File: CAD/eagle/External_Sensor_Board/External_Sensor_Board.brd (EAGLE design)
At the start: 50.8 x 33 mm, 12 parts, among them J1 SFW15R_FFC, U1 MAX31725MTA+, U2 HSCMNNN1.6BAAA3

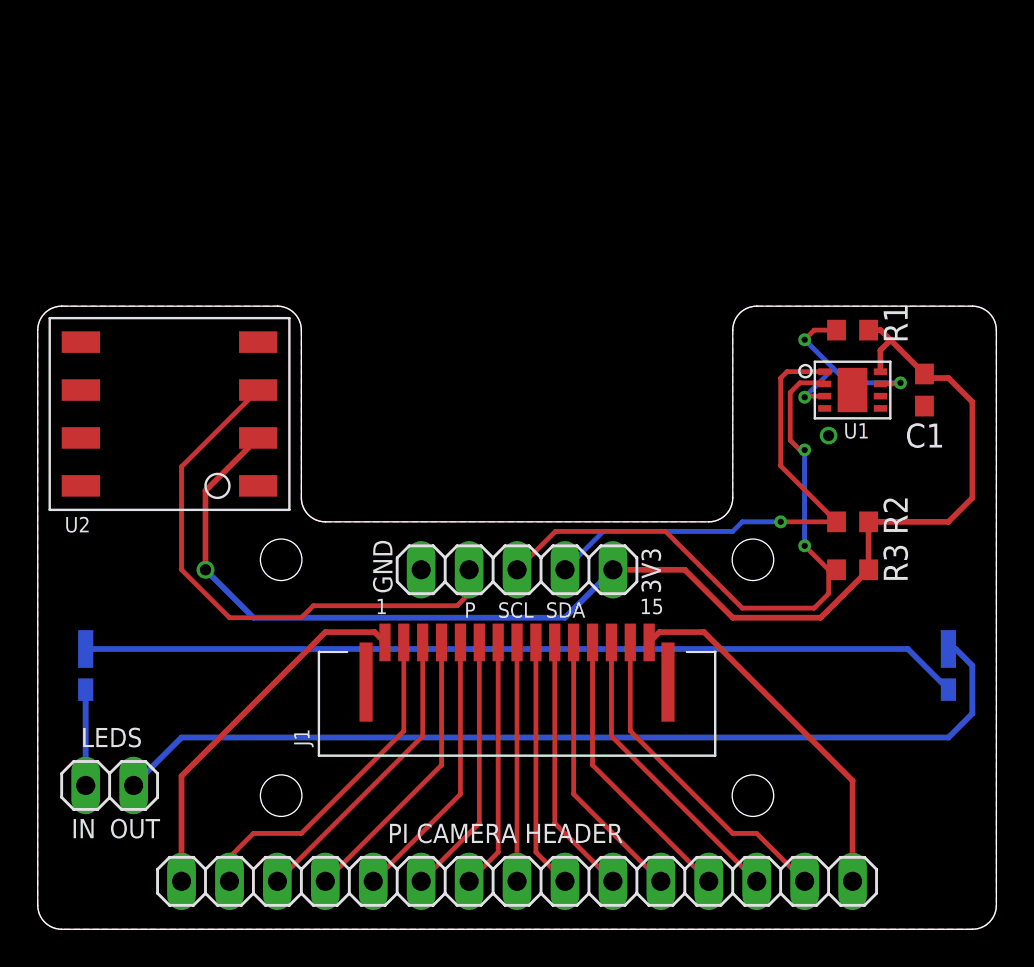
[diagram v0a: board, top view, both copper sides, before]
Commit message: Fixed dumb mistake on external sensor board, screw holes are now right distance apart. Rerouted around hole placement and verfied that DRC was still okay.
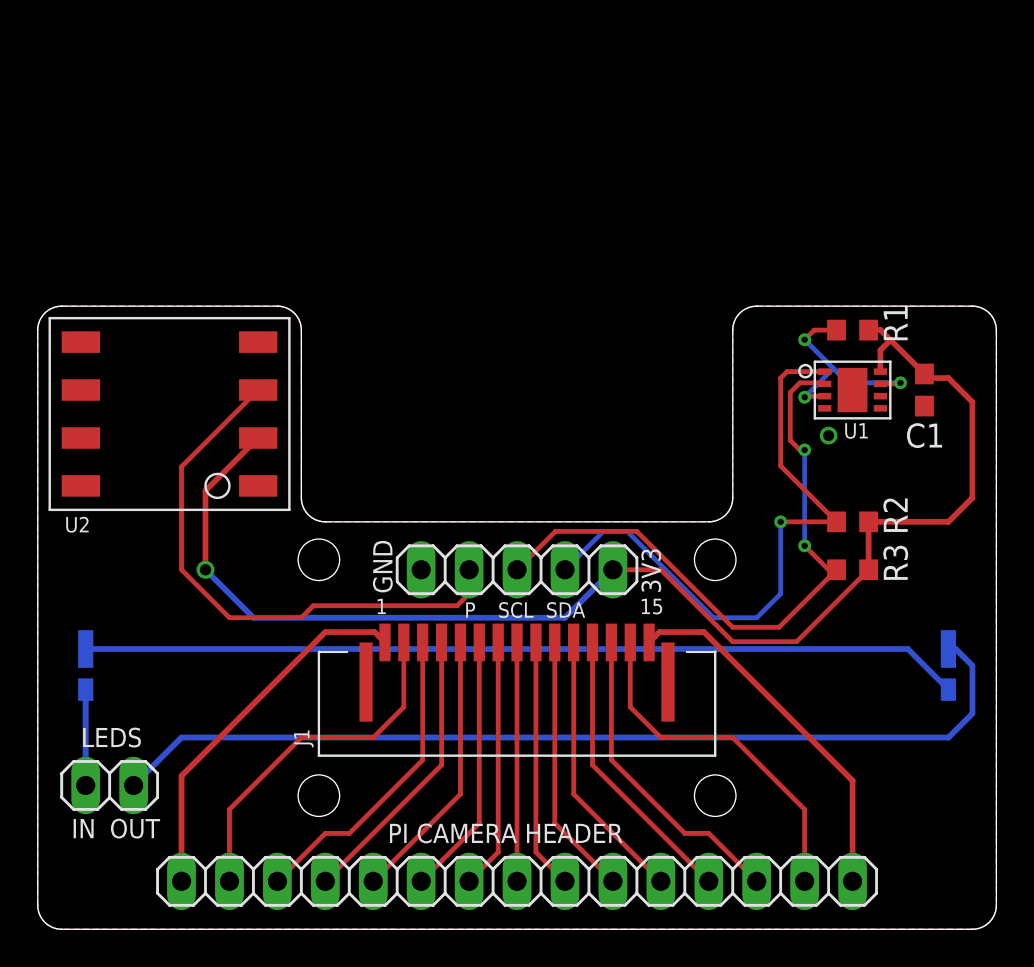
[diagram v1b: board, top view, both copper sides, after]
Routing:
- net SDA: track 26.8 -> 32.8 mm
- net CAM_SDA: track 17.2 -> 18.7 mm
- net +3V3: track 70.1 -> 71.2 mm
- net CAM_DP0: track 15.8 -> 16.6 mm
- net CAM_DN0: track 18.0 -> 18.7 mm
- net CAM_SCL: track 15.8 -> 16.6 mm
- net SCL: track 33.5 -> 34.0 mm
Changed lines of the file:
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@@
 <setting verticaltext="up"/>
 </settings>
-<grid distance="0.05" unitdist="inch" unit="mm" style="lines" multiple="1" display="yes" altdistance="0.01" altunitdist="inch" altunit="inch"/>
+<grid distance="0.05" unitdist="inch" unit="inch" style="lines" multiple="1" display="yes" altdistance="0.01" altunitdist="inch" altunit="inch"/>
 <layers>
 <layer number="1" name="Top" color="4" fill="1" visible="yes" active="yes"/>
@@
 <wire x1="12.7" y1="33.02" x2="1.27" y2="33.02" width="0" layer="20"/>
 <wire x1="1.27" y1="33.02" x2="0" y2="31.75" width="0" layer="20" curve="90"/>
-<hole x="12.9" y="19.58" drill="2.2"/>
-<hole x="37.9" y="19.58" drill="2.2"/>
-<hole x="37.9" y="7.08" drill="2.2"/>
-<hole x="12.9" y="7.08" drill="2.2"/>
+<hole x="14.89836875" y="19.58" drill="2.2"/>
+<hole x="35.90163125" y="19.58" drill="2.2"/>
+<hole x="35.90163125" y="7.08" drill="2.2"/>
+<hole x="14.89836875" y="7.08" drill="2.2"/>
 <wire x1="15.24" y1="21.59" x2="35.56" y2="21.59" width="0" layer="20"/>
 <wire x1="35.56" y1="21.59" x2="36.83" y2="22.86" width="0" layer="20" curve="90"/>
@@
 <wire x1="11.43" y1="16.51" x2="27.94" y2="16.51" width="0.3048" layer="16"/>
 <wire x1="27.94" y1="16.51" x2="30.48" y2="19.05" width="0.3048" layer="16"/>
-<wire x1="30.48" y1="19.05" x2="34.29" y2="19.05" width="0.3048" layer="1"/>
-<wire x1="34.29" y1="19.05" x2="36.83" y2="16.51" width="0.3048" layer="1"/>
-<wire x1="36.83" y1="16.51" x2="41.49" y2="16.51" width="0.3048" layer="1"/>
-<wire x1="41.49" y1="16.51" x2="44.03" y2="19.05" width="0.3048" layer="1"/>
 <wire x1="44.03" y1="19.05" x2="44.03" y2="21.59" width="0.3048" layer="1"/>
 <wire x1="44.03" y1="21.59" x2="48.26" y2="21.59" width="0.3048" layer="1"/>
@@
 <wire x1="44.655" y1="29.55" x2="44.655" y2="30.685" width="0.3048" layer="1"/>
 <wire x1="44.655" y1="30.685" x2="45.1925" y2="31.2225" width="0.3048" layer="1"/>
+<wire x1="30.48" y1="19.05" x2="33.02" y2="19.05" width="0.254" layer="1"/>
+<wire x1="33.02" y1="19.05" x2="36.83" y2="15.24" width="0.254" layer="1"/>
+<wire x1="36.83" y1="15.24" x2="40.22" y2="15.24" width="0.254" layer="1"/>
+<wire x1="40.22" y1="15.24" x2="44.03" y2="19.05" width="0.254" layer="1"/>
 </signal>
 <signal name="GND">
@@
 <contactref element="R2" pad="2"/>
 <contactref element="JP1" pad="2"/>
-<wire x1="27.94" y1="19.05" x2="29.972" y2="21.082" width="0.254" layer="16"/>
-<wire x1="29.972" y1="21.082" x2="36.83" y2="21.082" width="0.254" layer="16"/>
-<wire x1="36.83" y1="21.082" x2="37.338" y2="21.59" width="0.254" layer="16"/>
-<wire x1="37.338" y1="21.59" x2="39.37" y2="21.59" width="0.254" layer="16"/>
 <via x="39.37" y="21.59" extent="1-16" drill="0.3302"/>
 <wire x1="39.37" y1="21.59" x2="42.33" y2="21.59" width="0.254" layer="1"/>
@@
 <wire x1="39.37" y1="29.21" x2="39.71" y2="29.55" width="0.254" layer="1"/>
 <wire x1="39.71" y1="29.55" x2="41.705" y2="29.55" width="0.254" layer="1"/>
+<wire x1="27.94" y1="19.05" x2="29.972" y2="21.082" width="0.254" layer="16"/>
+<wire x1="29.972" y1="21.082" x2="31.242" y2="21.082" width="0.254" layer="16"/>
+<wire x1="31.242" y1="21.082" x2="35.814" y2="16.51" width="0.254" layer="16"/>
+<wire x1="35.814" y1="16.51" x2="38.1" y2="16.51" width="0.254" layer="16"/>
+<wire x1="38.1" y1="16.51" x2="39.37" y2="17.78" width="0.254" layer="16"/>
+<wire x1="39.37" y1="17.78" x2="39.37" y2="21.59" width="0.254" layer="16"/>
 </signal>
 <signal name="SCL">
@@
 <wire x1="41.649" y1="28.956" x2="41.705" y2="28.9" width="0.254" layer="1"/>
 <wire x1="40.64" y1="20.32" x2="41.91" y2="19.05" width="0.254" layer="1"/>
-<wire x1="41.91" y1="19.05" x2="41.91" y2="17.78" width="0.254" layer="1"/>
-<wire x1="41.91" y1="17.78" x2="41.148" y2="17.018" width="0.254" layer="1"/>
-<wire x1="41.148" y1="17.018" x2="37.338" y2="17.018" width="0.254" layer="1"/>
-<wire x1="37.338" y1="17.018" x2="33.274" y2="21.082" width="0.254" layer="1"/>
-<wire x1="33.274" y1="21.082" x2="27.432" y2="21.082" width="0.254" layer="1"/>
-<wire x1="27.432" y1="21.082" x2="25.4" y2="19.05" width="0.254" layer="1"/>
+<wire x1="25.4" y1="19.05" x2="27.432" y2="21.082" width="0.254" layer="1"/>
+<wire x1="27.432" y1="21.082" x2="31.75" y2="21.082" width="0.254" layer="1"/>
+<wire x1="31.75" y1="21.082" x2="36.83" y2="16.002" width="0.254" layer="1"/>
+<wire x1="36.83" y1="16.002" x2="39.282" y2="16.002" width="0.254" layer="1"/>
+<wire x1="39.282" y1="16.002" x2="42.33" y2="19.05" width="0.254" layer="1"/>
 </signal>
 <signal name="N$1">
@@
 <contactref element="J1" pad="14"/>
 <contactref element="JP2" pad="14"/>
-<wire x1="40.64" y1="2.54" x2="38.1" y2="5.08" width="0.254" layer="1"/>
-<wire x1="38.1" y1="5.08" x2="36.83" y2="5.08" width="0.254" layer="1"/>
-<wire x1="36.83" y1="5.08" x2="31.4" y2="10.51" width="0.254" layer="1"/>
-<wire x1="31.4" y1="10.51" x2="31.4" y2="15.2" width="0.254" layer="1"/>
+<wire x1="31.4" y1="15.2" x2="31.4" y2="11.78" width="0.254" layer="1"/>
+<wire x1="31.4" y1="11.78" x2="33.02" y2="10.16" width="0.254" layer="1"/>
+<wire x1="33.02" y1="10.16" x2="36.83" y2="10.16" width="0.254" layer="1"/>
+<wire x1="36.83" y1="10.16" x2="40.64" y2="6.35" width="0.254" layer="1"/>
+<wire x1="40.64" y1="6.35" x2="40.64" y2="2.54" width="0.254" layer="1"/>
 </signal>
 <signal name="CAM_SCL">
 <contactref element="J1" pad="13"/>
 <contactref element="JP2" pad="13"/>
-<wire x1="38.1" y1="2.54" x2="30.4" y2="10.24" width="0.254" layer="1"/>
-<wire x1="30.4" y1="10.24" x2="30.4" y2="15.2" width="0.254" layer="1"/>
+<wire x1="30.4" y1="15.2" x2="30.4" y2="8.97" width="0.254" layer="1"/>
+<wire x1="30.4" y1="8.97" x2="34.29" y2="5.08" width="0.254" layer="1"/>
+<wire x1="34.29" y1="5.08" x2="35.56" y2="5.08" width="0.254" layer="1"/>
+<wire x1="35.56" y1="5.08" x2="38.1" y2="2.54" width="0.254" layer="1"/>
 </signal>
 <signal name="CAM_GPIO1">
@@
 <contactref element="J1" pad="3"/>
 <contactref element="JP2" pad="3"/>
-<wire x1="12.7" y1="2.54" x2="20.4" y2="10.24" width="0.254" layer="1"/>
-<wire x1="20.4" y1="10.24" x2="20.4" y2="15.2" width="0.254" layer="1"/>
+<wire x1="20.4" y1="15.2" x2="20.4" y2="8.97" width="0.254" layer="1"/>
+<wire x1="20.4" y1="8.97" x2="16.51" y2="5.08" width="0.254" layer="1"/>
+<wire x1="16.51" y1="5.08" x2="15.24" y2="5.08" width="0.254" layer="1"/>
+<wire x1="15.24" y1="5.08" x2="12.7" y2="2.54" width="0.254" layer="1"/>
 </signal>
 <signal name="CAM_DN0">
 <contactref element="J1" pad="2"/>
 <contactref element="JP2" pad="2"/>
-<wire x1="19.4" y1="15.2" x2="19.4" y2="10.51" width="0.254" layer="1"/>
-<wire x1="19.4" y1="10.51" x2="13.97" y2="5.08" width="0.254" layer="1"/>
-<wire x1="13.97" y1="5.08" x2="11.43" y2="5.08" width="0.254" layer="1"/>
-<wire x1="11.43" y1="5.08" x2="10.16" y2="3.81" width="0.254" layer="1"/>
-<wire x1="10.16" y1="3.81" x2="10.16" y2="2.54" width="0.254" layer="1"/>
+<wire x1="19.4" y1="15.2" x2="19.4" y2="11.78" width="0.254" layer="1"/>
+<wire x1="19.4" y1="11.78" x2="17.78" y2="10.16" width="0.254" layer="1"/>
+<wire x1="17.78" y1="10.16" x2="13.97" y2="10.16" width="0.254" layer="1"/>
+<wire x1="13.97" y1="10.16" x2="10.16" y2="6.35" width="0.254" layer="1"/>
+<wire x1="10.16" y1="6.35" x2="10.16" y2="2.54" width="0.254" layer="1"/>
 </signal>
 <signal name="LED_IN">
